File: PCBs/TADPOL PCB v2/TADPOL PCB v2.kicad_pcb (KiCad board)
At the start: 2 copper layers, 70 x 50 mm, 23 parts, among them J1 Lora Radio, J10 Nichrome, J11 Battery In, J13 Bypass, J2 Magnetic Connector, J3 Live Video, J4 I2C Connector, J5 Telemetry GPIO, J6 Telemetry Data, J7 Servo 1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

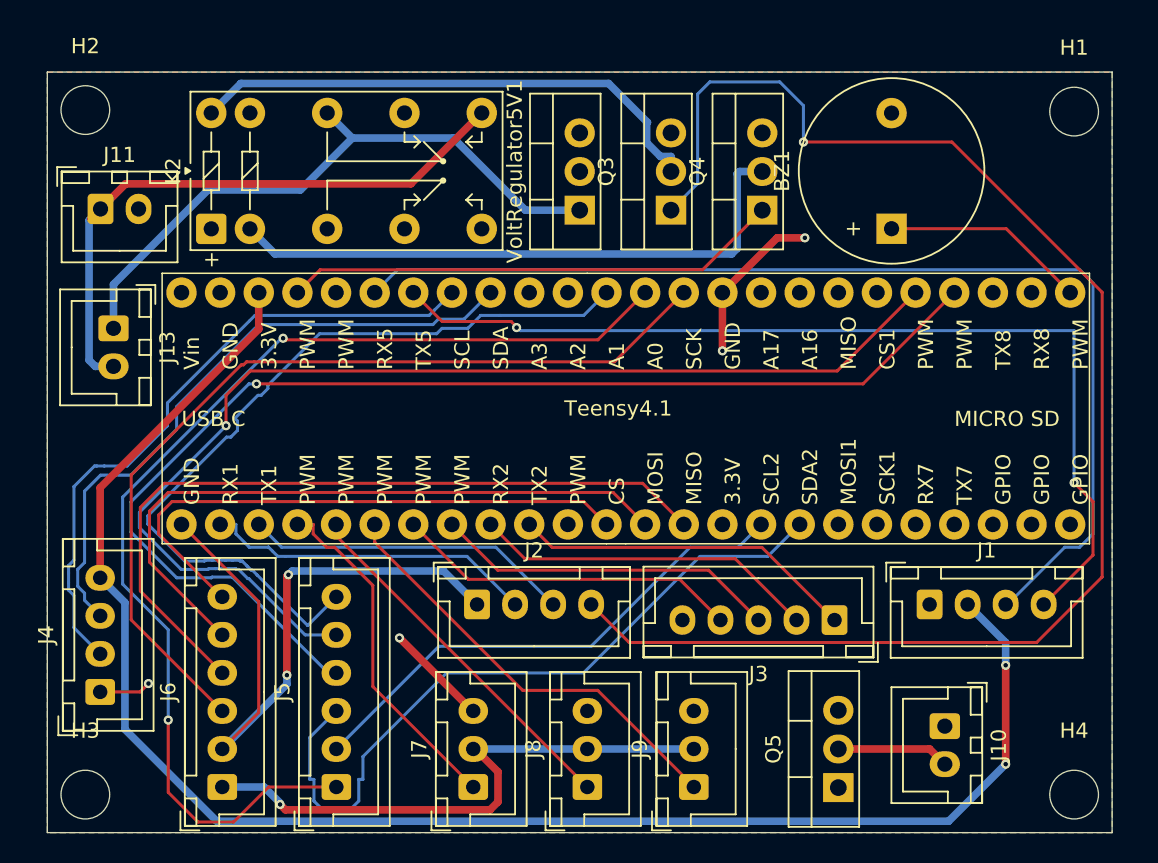
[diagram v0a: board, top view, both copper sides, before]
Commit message: fixed traces
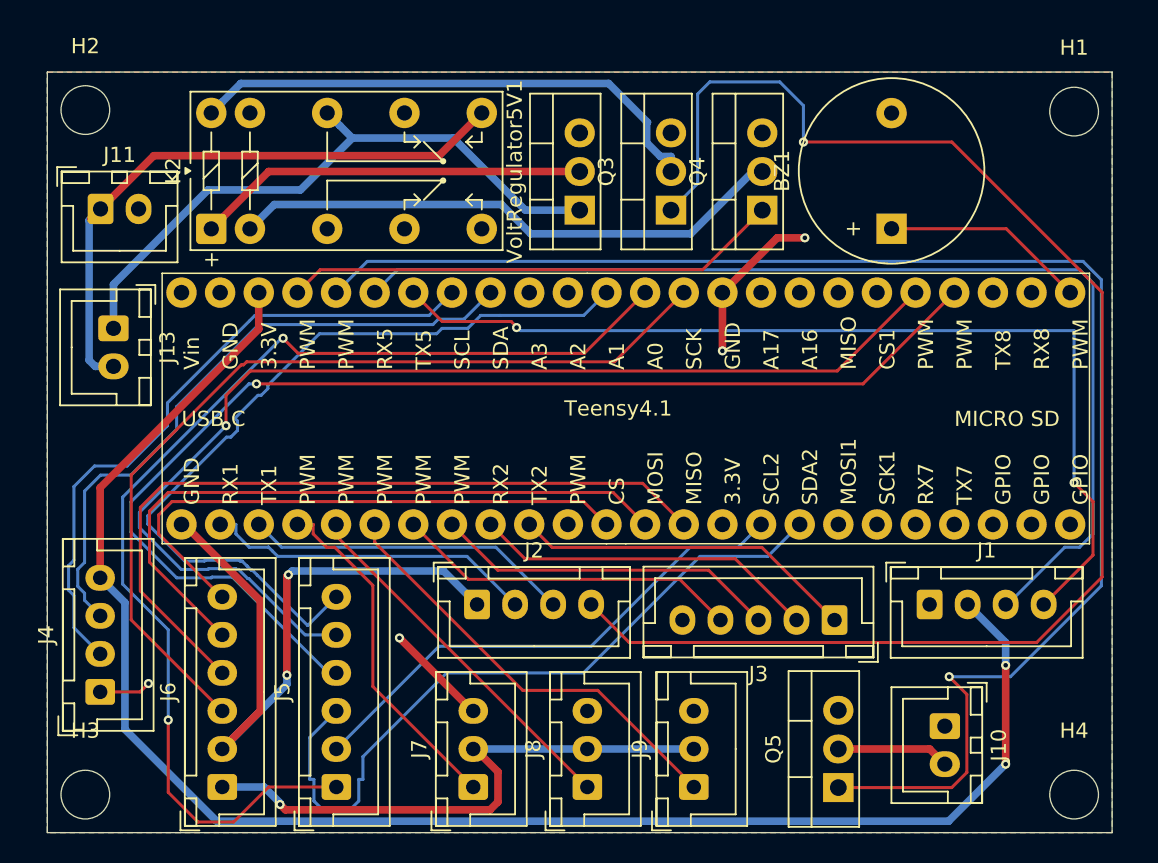
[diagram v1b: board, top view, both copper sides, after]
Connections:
- Teensy4.1 pad 43: unconnected-(Teensy4.1-PWM-Pad43) -> Nichrome_1
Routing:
- net Nichrome_1: track 0.00 -> 99.9 mm, vias 0 -> 1
- net GND: track 65.5 -> 91.5 mm
- net Net-(Q4-D): track 39.5 -> 36.8 mm
- net Net-(J13-Pin_1): track 41.8 -> 43.0 mm
- net Net-(Q3-D): track 34.9 -> 35.9 mm
- net IRQ: track 73.5 -> 74.2 mm

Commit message: fixed Gaia Board
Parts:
- removed J10: Nichrome, Connector_JST:JST_XH_B2B-XH-A_1x02_P2.50mm_Vertical
- removed J9: Servo 3, Connector_JST:JST_XH_B3B-XH-A_1x03_P2.50mm_Vertical
- removed Q3: Vehicle On, Package_TO_SOT_THT:TO-220-3_Vertical
- removed Q4: Vehicle Off, Package_TO_SOT_THT:TO-220-3_Vertical
- removed Q5: Nichrome, Package_TO_SOT_THT:TO-220-3_Vertical
- added J12: Vehicle Off, Connector_JST:JST_XH_B2B-XH-A_1x02_P2.50mm_Vertical, F.Cu at (112.5, 45.5)
- J4: value I2C Connector -> Sensor Board
- moved H3 79.1 mm to (174.0, 38.0)
- moved H4 79.1 mm to (109.0, 38.0)
- moved H2 76.1 mm to (174.0, 77.5)
- moved H1 76.0 mm to (109.0, 77.5)
- moved J5 40.7 mm to (166.0, 78.0), turned to 180 degrees
- moved J11 37.0 mm to (147.0, 43.5), turned to 90 degrees
- moved J6 29.3 mm to (147.0, 78.0), turned to 180 degrees
- moved J2 23.8 mm to (111.0, 70.0)
- moved J7 12.3 mm to (130.0, 71.0), turned to 180 degrees
- moved J8 11.5 mm to (141.5, 71.0), turned to 180 degrees
- moved J4 10.6 mm to (120.5, 77.0), turned to 0 degrees
- moved BZ1 2.50 mm to (164.5, 45.8)
- moved J3 0.92 mm to (157.5, 71.0)
- moved J1 0.71 mm to (164.0, 70.0)
- moved J13 0.49 mm to (110.5, 52.0)
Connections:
- J13 pad 1: Net-(J13-Pin_1) -> +5V
- J13 pad 2: VIN -> Net-(J13-Pin_2)
- K2 pad 21: Net-(J13-Pin_1) -> +5V
- K2 pad 24: VIN -> Net-(J13-Pin_2)
- K2 pad A1: GND -> Vehicle_On
- K2 pad A2: Net-(Q3-D) -> GND
- K2 pad B1: Net-(Q4-D) -> +5V
- K2 pad B2: GND -> Vehicle_Off
- Teensy4.1 pad 44: Vehicle_Off -> unconnected-(Teensy4.1-PWM-Pad44)
- VoltRegulator5V1 pad 1: Net-(J13-Pin_1) -> VIN
- VoltRegulator5V1 pad 3: +5V -> Net-(J13-Pin_2)
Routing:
- net Nichrome_1: track 99.9 -> 0.00 mm, vias 1 -> 0
- net GND: track 91.5 -> 26.6 mm, vias 6 -> 0
- net Vehicle_On: track 97.5 -> 35.9 mm, vias 1 -> 2
- net Net-(J13-Pin_1): track 43.0 -> 0.00 mm
- net Net-(J13-Pin_2): track 0.00 -> 40.5 mm
- net Net-(Q4-D): track 36.8 -> 0.00 mm
- net Net-(Q3-D): track 35.9 -> 0.00 mm
- net VIN: track 40.6 -> 5.95 mm
- net MISO: track 50.6 -> 17.1 mm
- net +5V: track 37.7 -> 5.65 mm, vias 1 -> 0
- net GPIO2: track 79.2 -> 47.1 mm
- net GPIO1: track 48.8 -> 18.4 mm
- net PWM_SERVO3: track 28.8 -> 0.00 mm
- net MOSI: track 44.1 -> 17.1 mm
- net GPIO3: track 75.1 -> 49.7 mm
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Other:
- board size 70 x 50 mm -> 71 x 45.5 mm
